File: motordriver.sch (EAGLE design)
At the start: 81 parts, among them J1 CONNECTOR_MOTORS, J2 CONNECTOR_MOTORS, J3 CONNECTOR_MOTORS, J4 CONNECTOR_MOTORS, J5 HEADER_1X3, J6 HEADER_1X3, Q1 MOSFET, Q10 MOSFET, Q11 MOSFET, Q12 MOSFET, Q13 MOSFET, Q14 MOSFET, Q15 MOSFET, Q16 MOSFET, Q2 MOSFET, Q3 MOSFET, Q4 MOSFET, Q5 MOSFET, Q6 MOSFET, Q7 MOSFET, Q8 MOSFET, Q9 MOSFET, U1 74XX139_PDIP, U10 IR2111_PDIP, U11 IR2111_PDIP, U2 TL084_PDIP, U3 7812_TO220, U4 IR2111_PDIP, U5 IR2111_PDIP, U6 IR2111_PDIP, U7 IR2111_PDIP, U8 IR2111_PDIP, U9 IR2111_PDIP

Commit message: changed schematic
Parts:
- added C17, C18, C25: CAP_330U_25V, motordriverslib:CAP_330U_25V
- added J7, J8: HEADER_1X3, motordriverslib:HEADER_1X3
- added U$2: CONN_5X2, motordriverslib:CONN_5X2
- added U12: 7812_TO220, motordriverslib:7812_TO220
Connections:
- removed net N$2: U2.3+, U2.4+
- removed net N$28: J6.3
- removed net N$29: J6.2
- removed net N$3: U2.1+, U2.2+
- new net VCC_12V_ALT: C17.+, J5.2, J6.2, U12.OUT
- new net VCC_5V: C18.+, U$1.OUT, U1.P$16
- new net X_DIR: J7.1, U1.P$3
- new net X_EN: J7.2, U1.P$2
- new net X_IN: J7.3, U1.P$1
- new net Y_DIR: J8.1, U1.P$13
- new net Y_EN: J8.2, U1.P$14
- new net Y_IN: J8.3, U1.P$15
- net GND: now also C17.-, C18.-, C25.-, U12.GND
- net N$1: now also U7.P$2; no longer U1.P$11, U2.4-
- net N$10: no longer U2.OUT4, U6.P$2
- net N$11: now also U1.P$11; no longer U$1.OUT, U1.P$16, U2.VCC
- net N$12: now also U1.P$7; no longer J5.2
- net N$23: now also U1.P$9; no longer J5.3
- net N$4: now also U6.P$2; no longer U1.P$5, U2.1-
- net N$44: no longer U2.OUT1, U9.P$2
- net N$5: now also U10.P$2; no longer U1.P$7, U2.2-
- net N$6: now also U9.P$2; no longer U1.P$9, U2.3-
- net N$63: no longer U10.P$2, U2.OUT2
- net N$7: no longer U2.OUT3, U7.P$2
- net N$8: now also U1.P$5; no longer U$1.IN
- net VCC_12V: now also C25.+, U2.VCC
- net V_IN: now also U$1.IN, U12.IN
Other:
- note added: "12 V AUX LDO"
- note added: "CONTROLLER X IN"
- note added: "CONTROLLER Y IN"
- note added: "ENCODER INPUTS (NEED PULLUPS)"
- note added: "MOTOR DRIVER 1"
- note added: "MOTOR DRIVER 2"
- note added: "MOTOR DRIVER 3"
- note added: "MOTOR DRIVER 4"
- moved on the sheet: J5, J6, U$1

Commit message: Finished schematic
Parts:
- removed C10, C14, C16, C20, C8: CAP_2200U_63V, motordriverslib:CAP_2200U_63V
- removed D1, D2, D3, D4, D5, D6, D8: 1N4004, diode:1N4004
- added C26, C27, C28, C29, C30, C31, C32: CAP_330N_50V, motordriverslib:CAP_330N_50V
- added D10, D11, D12, D13, D14, D15, D9: 1N4148, motordriverslib:1N4148
- added J10, J11: HEADER_1X3, motordriverslib:HEADER_1X3
- added J9: CONNECTOR_MOTORS, motordriverslib:CONNECTOR_MOTORS
- added R17, R18, R19, R20, R21, R22: RES_SMT, motordriverslib:RES_SMT
- C2, C4: value CAP_2200U_63V -> CAP_1U; device motordriverslib:CAP_2200U_63V -> motordriverslib:CAP_1U
- C22: value CAP_2200U_63V -> CAP_330N_50V; device motordriverslib:CAP_2200U_63V -> motordriverslib:CAP_330N_50V
- D7: value 1N4004 -> 1N4148; device diode:1N4004 -> motordriverslib:1N4148
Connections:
- removed net N$10: U5.P$2
- removed net N$11: U1.P$11
- removed net N$12: U1.P$7
- removed net N$23: U1.P$9
- removed net N$35: R8.1, U6.P$4
- removed net N$4: U6.P$2
- removed net N$44: U11.P$2
- removed net N$5: U10.P$2
- removed net N$52: R12.1, U8.P$4
- removed net N$58: R11.1, U9.P$4
- removed net N$6: U9.P$2
- removed net N$63: U8.P$2
- removed net N$7: U4.P$2
- removed net N$8: U1.P$5
- new net N$2: R8.1, U7.P$4
- new net N$29: R11.1, U8.P$4
- new net REF_3V: R17.1, R18.2, U2.1+, U2.2+, U2.3+, U2.4+
- new net VIN_RAW: J9.+, S1.+
- new net X_A: J10.3, R19.1, U$2.P$4
- new net X_B: J10.2, R20.1, U$2.P$5
- new net X_PWM_A: U11.P$2, U2.OUT1, U9.P$2
- new net X_PWM_A_RAW: U1.P$5, U2.1-
- new net X_PWM_B: U10.P$2, U2.OUT2, U8.P$2
- new net X_PWM_B_RAW: U1.P$7, U2.2-
- new net Y_A: J11.3, R21.1, U$2.P$7
- new net Y_B: J11.2, R22.1, U$2.P$6
- new net Y_PWM_A: U2.OUT4, U4.P$2, U7.P$2
- new net Y_PWM_A_RAW: U1.P$11, U2.4-
- new net Y_PWM_B: U2.OUT3, U5.P$2, U6.P$2
- new net Y_PWM_B_RAW: U1.P$9, U2.3-
- net GND: now also C2.2, C4.2, J10.1, J11.1, J9.-, R18.1, U$2.P$1, U$2.P$10
- net N$1: now also R12.1, U9.P$4; no longer U7.P$2
- net N$13: now also C29.+, D15.C; no longer C2.+, D1.C
- net N$15: now also C29.-; no longer C2.-
- net N$19: now also U4.P$4; no longer U5.P$4
- net N$20: now also U5.P$4; no longer U4.P$4
- net N$25: now also C30.+, D14.C; no longer C4.+, D2.C
- net N$26: now also C30.-; no longer C4.-
- net N$30: now also C32.+, D12.C; no longer C8.+, D3.C
- net N$31: now also C32.-; no longer C8.-
- net N$38: now also C31.+, D13.C; no longer C10.+, D4.C
- net N$39: now also C31.-; no longer C10.-
- net N$41: now also U6.P$4; no longer U7.P$4
- net N$47: now also C27.+, D11.C; no longer C14.+, D5.C
- net N$48: now also C27.-; no longer C14.-
- net N$55: now also C28.+, D10.C; no longer C16.+, D6.C
- net N$56: now also C28.-; no longer C16.-
- net N$64: now also C26.+; no longer C20.+
- net N$65: now also C26.-; no longer C20.-
- net N$72: now also D9.C; no longer D8.C
- net VCC_12V: now also C2.1, D10.A, D11.A, D12.A, D13.A, D14.A, D15.A, D9.A; no longer D1.A, D2.A, D3.A, D4.A, D5.A, D6.A, D8.A, Q10.D, Q12.D, Q14.D, Q16.D, Q2.D, Q4.D, Q6.D, Q8.D, S1.+
- net VCC_5V: now also C4.1, R17.2, R19.2, R20.2, R21.2, R22.2, U$2.P$2, U$2.P$9
- net V_IN: now also Q10.D, Q12.D, Q14.D, Q16.D, Q2.D, Q4.D, Q6.D, Q8.D
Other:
- note added: "10k"
- note added: "3V COMP REFERENCE"
- note added: "6.6k"
- note added: "DRIVERS 1&2 ARE LINKED"
- note added: "DRIVERS 3&4 ARE LINKED"
- note added: "ENCODER OUTPUTS TO CONTROLLER"
- note added: "FAN OUTPUTS"
- note added: "INPUT POWER SYSTEM"
- note added: "INPUT VOLTAGE PORT"
- note added: "X"
- note added: "Y"
- moved on the sheet: C1, C12, C13, C15, C17, C18, C19, C21, C22, C23, C24, C25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

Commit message: HumDdunm
slight changes
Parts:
- added D1: LED_SMT, motordriverslib:LED_SMT
- added R23: RES_SMT, motordriverslib:RES_SMT
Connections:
- new net N$4: D1.C, R23.2
- new net N$6: R23.1
- net VCC_12V: now also D1.A
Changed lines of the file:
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@@
 <?xml version="1.0" encoding="utf-8"?>
 <!DOCTYPE eagle SYSTEM "eagle.dtd">
-<eagle version="7.1.0">
+<eagle version="7.2.0">
 <drawing>
 <settings>
@@
 <part name="R21" library="motordriverslib" deviceset="RES_SMT" device=""/>
 <part name="R22" library="motordriverslib" deviceset="RES_SMT" device=""/>
+<part name="D1" library="motordriverslib" deviceset="LED_SMT" device=""/>
+<part name="R23" library="motordriverslib" deviceset="RES_SMT" device=""/>
+<part name="GND32" library="supply1" deviceset="GND" device=""/>
 </parts>
 <sheets>
@@
 <instance part="R21" gate="G$1" x="-20.32" y="-86.36" rot="R90"/>
 <instance part="R22" gate="G$1" x="-5.08" y="-88.9" rot="R90"/>
+<instance part="D1" gate="G$1" x="-73.66" y="127"/>
+<instance part="R23" gate="G$1" x="-73.66" y="114.3" rot="R90"/>
+<instance part="GND32" gate="1" x="-73.66" y="99.06"/>
 </instances>
 <busses>
@@
 <wire x1="-203.2" y1="43.18" x2="-190.5" y2="43.18" width="0.1524" layer="91"/>
 <label x="-205.74" y="43.18" size="1.778" layer="95"/>
+</segment>
+<segment>
+<pinref part="D1" gate="G$1" pin="A"/>
+<wire x1="-73.66" y1="132.08" x2="-73.66" y2="134.62" width="0.1524" layer="91"/>
+<label x="-76.2" y="134.62" size="1.778" layer="95" rot="R90"/>
 </segment>
 </net>
@@
 <wire x1="-15.24" y1="-96.52" x2="-15.24" y2="-101.6" width="0.1524" layer="91"/>
 </segment>
+<segment>
+<pinref part="GND32" gate="1" pin="GND"/>
+<wire x1="-73.66" y1="106.68" x2="-73.66" y2="101.6" width="0.1524" layer="91"/>
+</segment>
 </net>
 <net name="N$13" class="0">
@@
 </segment>
 </net>
+<net name="N$4" class="0">
+<segment>
+<pinref part="D1" gate="G$1" pin="C"/>
+<pinref part="R23" gate="G$1" pin="2"/>
+<wire x1="-73.66" y1="124.46" x2="-73.66" y2="119.38" width="0.1524" layer="91"/>
+</segment>
+</net>
+<net name="N$6" class="0">
+<segment>
+<pinref part="R23" gate="G$1" pin="1"/>
+<wire x1="-73.66" y1="109.22" x2="-73.66" y2="106.68" width="0.1524" layer="91"/>
+</segment>
+</net>

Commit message: Created board.
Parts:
- renumbered C28 to C8
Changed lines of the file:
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@@
 <?xml version="1.0" encoding="utf-8"?>
 <!DOCTYPE eagle SYSTEM "eagle.dtd">
-<eagle version="7.2.0">
+<eagle version="7.1.0">
 <drawing>
 <settings>
@@
 <part name="C26" library="motordriverslib" deviceset="CAP_330N_50V" device=""/>
 <part name="C27" library="motordriverslib" deviceset="CAP_330N_50V" device=""/>
-<part name="C28" library="motordriverslib" deviceset="CAP_330N_50V" device=""/>
 <part name="C29" library="motordriverslib" deviceset="CAP_330N_50V" device=""/>
 <part name="C30" library="motordriverslib" deviceset="CAP_330N_50V" device=""/>
@@
 <part name="R23" library="motordriverslib" deviceset="RES_SMT" device=""/>
 <part name="GND32" library="supply1" deviceset="GND" device=""/>
+<part name="C8" library="motordriverslib" deviceset="CAP_330N_50V" device=""/>
 </parts>
 <sheets>
@@
 <instance part="C26" gate="G$1" x="-434.34" y="-20.32"/>
 <instance part="C27" gate="G$1" x="-434.34" y="58.42"/>
-<instance part="C28" gate="G$1" x="-269.24" y="55.88"/>
 <instance part="C29" gate="G$1" x="-30.48" y="53.34"/>
 <instance part="C30" gate="G$1" x="137.16" y="50.8"/>
@@
 <instance part="R23" gate="G$1" x="-73.66" y="114.3" rot="R90"/>
 <instance part="GND32" gate="1" x="-73.66" y="99.06"/>
+<instance part="C8" gate="G$1" x="-269.24" y="55.88"/>
 </instances>
 <busses>
@@
 <wire x1="-279.4" y1="63.5" x2="-269.24" y2="63.5" width="0.1524" layer="91"/>
 <junction x="-269.24" y="63.5"/>
-<pinref part="C28" gate="G$1" pin="+"/>
 <pinref part="D10" gate="G$1" pin="C"/>
+<pinref part="C8" gate="G$1" pin="+"/>
 </segment>
 </net>
@@
 <pinref part="U9" gate="G$1" pin="P$6"/>
 <wire x1="-269.24" y1="48.26" x2="-279.4" y2="48.26" width="0.1524" layer="91"/>
-<pinref part="C28" gate="G$1" pin="-"/>
-</segment>
-</net>
+<pinref part="C8" gate="G$1" pin="-"/>
+</segment>
+</net>

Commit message: Cap23 just got murde
I put it in the dirt or somethin
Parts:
- removed C23: CAP_2200U_63V, motordriverslib:CAP_2200U_63V
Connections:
- net GND: no longer C23.-
- net VCC_12V: no longer C23.+
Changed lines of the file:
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@@
 <?xml version="1.0" encoding="utf-8"?>
 <!DOCTYPE eagle SYSTEM "eagle.dtd">
-<eagle version="7.1.0">
+<eagle version="7.2.0">
 <drawing>
 <settings>
@@
 <part name="S1" library="motordriverslib" deviceset="ROCKER_THRU" device=""/>
 <part name="U$1" library="motordriverslib" deviceset="7805_TO220" device=""/>
-<part name="P+12" library="supply1" deviceset="VCC" device=""/>
 <part name="P+13" library="supply1" deviceset="VCC" device=""/>
-<part name="C23" library="motordriverslib" deviceset="CAP_2200U_63V" device=""/>
 <part name="C24" library="motordriverslib" deviceset="CAP_2200U_63V" device=""/>
-<part name="GND12" library="supply1" deviceset="GND" device=""/>
 <part name="GND13" library="supply1" deviceset="GND" device=""/>
 <part name="GND6" library="supply1" deviceset="GND" device=""/>
@@
 <instance part="S1" gate="G$1" x="-203.2" y="104.14" rot="R270"/>
 <instance part="U$1" gate="G$1" x="-353.06" y="-78.74"/>
-<instance part="P+12" gate="VCC" x="-142.24" y="134.62"/>
 <instance part="P+13" gate="VCC" x="-109.22" y="134.62"/>
-<instance part="C23" gate="G$1" x="-142.24" y="121.92"/>
 <instance part="C24" gate="G$1" x="-109.22" y="121.92"/>
-<instance part="GND12" gate="1" x="-142.24" y="111.76"/>
 <instance part="GND13" gate="1" x="-109.22" y="111.76"/>
 <instance part="GND6" gate="1" x="-353.06" y="-96.52"/>
@@
 </segment>
 <segment>
-<pinref part="P+12" gate="VCC" pin="VCC"/>
-<pinref part="C23" gate="G$1" pin="+"/>
-<wire x1="-142.24" y1="132.08" x2="-142.24" y2="127" width="0.1524" layer="91"/>
-</segment>
-<segment>
 <pinref part="P+13" gate="VCC" pin="VCC"/>
 <pinref part="C24" gate="G$1" pin="+"/>
@@
 </segment>
 <segment>
-<pinref part="C23" gate="G$1" pin="-"/>
-<pinref part="GND12" gate="1" pin="GND"/>
-<wire x1="-142.24" y1="119.38" x2="-142.24" y2="114.3" width="0.1524" layer="91"/>
-</segment>
-<segment>

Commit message: More PCB tinkering
Routing will commence soon
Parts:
- removed S1: ROCKER_THRU, motordriverslib:ROCKER_THRU
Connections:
- net VIN_RAW: now also U3.IN; no longer S1.+
- net V_IN: no longer S1.-, U3.IN
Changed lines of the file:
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@@
 <?xml version="1.0" encoding="utf-8"?>
 <!DOCTYPE eagle SYSTEM "eagle.dtd">
-<eagle version="7.1.0">
+<eagle version="7.2.0">
 <drawing>
 <settings>
@@
 <part name="C11" library="motordriverslib" deviceset="CAP_1U" device=""/>
 <part name="C12" library="motordriverslib" deviceset="CAP_1U" device=""/>
-<part name="S1" library="motordriverslib" deviceset="ROCKER_THRU" device=""/>
 <part name="U$1" library="motordriverslib" deviceset="7805_TO220" device=""/>
 <part name="P+13" library="supply1" deviceset="VCC" device=""/>
@@
 <instance part="C11" gate="G$1" x="38.1" y="43.18" rot="R90"/>
 <instance part="C12" gate="G$1" x="38.1" y="-27.94" rot="R90"/>
-<instance part="S1" gate="G$1" x="-203.2" y="104.14" rot="R270"/>
 <instance part="U$1" gate="G$1" x="-353.06" y="-78.74"/>
 <instance part="P+13" gate="VCC" x="-109.22" y="134.62"/>
@@
 <net name="V_IN" class="0">
 <segment>
-<pinref part="U3" gate="G$1" pin="IN"/>
-<wire x1="-203.2" y1="93.98" x2="-193.04" y2="93.98" width="0.1524" layer="91"/>
-<pinref part="S1" gate="G$1" pin="-"/>
-<wire x1="-203.2" y1="96.52" x2="-203.2" y2="93.98" width="0.1524" layer="91"/>
-<label x="-200.66" y="93.98" size="1.778" layer="95"/>
-</segment>
-<segment>
 <pinref part="U$1" gate="G$1" pin="IN"/>
 <wire x1="-360.68" y1="-78.74" x2="-365.76" y2="-78.74" width="0.1524" layer="91"/>
@@
 <net name="VIN_RAW" class="0">
 <segment>
-<pinref part="S1" gate="G$1" pin="+"/>
-<wire x1="-203.2" y1="111.76" x2="-203.2" y2="116.84" width="0.1524" layer="91"/>
 <label x="-208.28" y="116.84" size="1.778" layer="95"/>
 <pinref part="J9" gate="G$1" pin="+"/>
 <wire x1="-226.06" y1="116.84" x2="-203.2" y2="116.84" width="0.1524" layer="91"/>
-</segment>
-</net>
+<pinref part="U3" gate="G$1" pin="IN"/>
+<wire x1="-203.2" y1="93.98" x2="-193.04" y2="93.98" width="0.1524" layer="91"/>
+<label x="-200.66" y="93.98" size="1.778" layer="95"/>
+<wire x1="-203.2" y1="116.84" x2="-203.2" y2="93.98" width="0.1524" layer="91"/>
+</segment>
+</net>

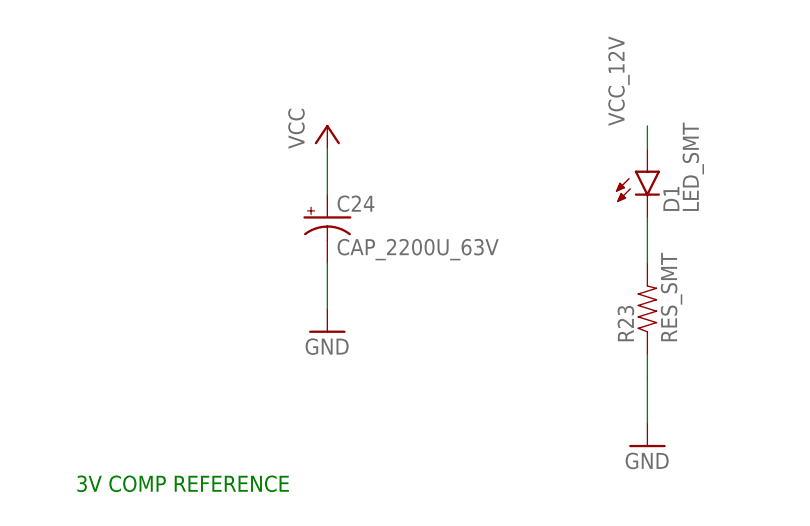
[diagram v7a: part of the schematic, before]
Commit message: Components arranged, 86'ed the 36V cap (fit ext.)
YEEEEEHAA it all fits. I will still be rearranging components, but
initially they all fit. Routing will happen later this afternoon.
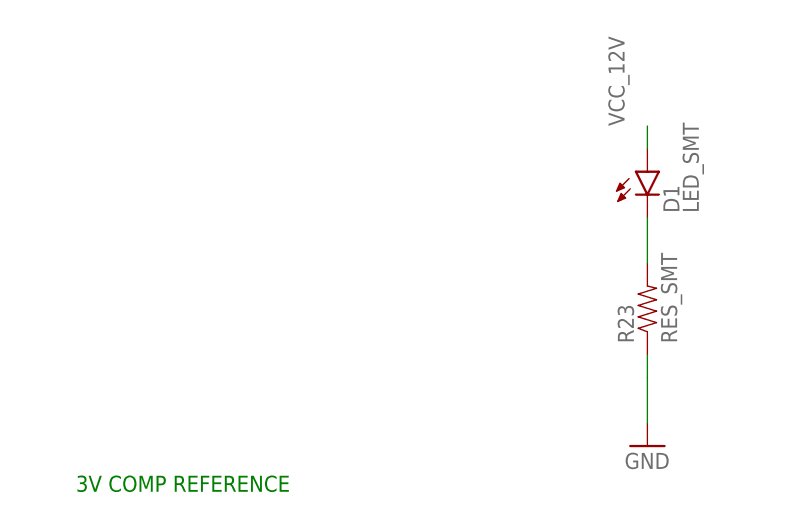
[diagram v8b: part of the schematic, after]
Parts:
- removed C24: CAP_2200U_63V, motordriverslib:CAP_2200U_63V
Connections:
- net GND: no longer C24.-
- net VCC_12V: no longer C24.+
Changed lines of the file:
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@@
 <part name="C12" library="motordriverslib" deviceset="CAP_1U" device=""/>
 <part name="U$1" library="motordriverslib" deviceset="7805_TO220" device=""/>
-<part name="P+13" library="supply1" deviceset="VCC" device=""/>
-<part name="C24" library="motordriverslib" deviceset="CAP_2200U_63V" device=""/>
-<part name="GND13" library="supply1" deviceset="GND" device=""/>
 <part name="GND6" library="supply1" deviceset="GND" device=""/>
 <part name="GND7" library="supply1" deviceset="GND" device=""/>
@@
 <instance part="C12" gate="G$1" x="38.1" y="-27.94" rot="R90"/>
 <instance part="U$1" gate="G$1" x="-353.06" y="-78.74"/>
-<instance part="P+13" gate="VCC" x="-109.22" y="134.62"/>
-<instance part="C24" gate="G$1" x="-109.22" y="121.92"/>
-<instance part="GND13" gate="1" x="-109.22" y="111.76"/>
 <instance part="GND6" gate="1" x="-353.06" y="-96.52"/>
 <instance part="GND7" gate="1" x="-190.5" y="-22.86"/>
@@
 </segment>
 <segment>
-<pinref part="P+13" gate="VCC" pin="VCC"/>
-<pinref part="C24" gate="G$1" pin="+"/>
-<wire x1="-109.22" y1="132.08" x2="-109.22" y2="127" width="0.1524" layer="91"/>
-</segment>
-<segment>
 <pinref part="U4" gate="G$1" pin="P$1"/>
 <wire x1="101.6" y1="63.5" x2="116.84" y2="63.5" width="0.1524" layer="91"/>
@@
 </segment>
 <segment>
-<pinref part="C24" gate="G$1" pin="-"/>
-<pinref part="GND13" gate="1" pin="GND"/>
-<wire x1="-109.22" y1="119.38" x2="-109.22" y2="114.3" width="0.1524" layer="91"/>
-</segment>
-<segment>
